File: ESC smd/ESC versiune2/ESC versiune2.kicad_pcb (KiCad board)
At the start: 2 copper layers, 115.8 x 79.8 mm, 96 parts, among them J1 Conn_01x03, J2 Conn_01x03, J3 Conn_01x03, J4 Conn_01x03, J5 Conn_01x02, J6 Conn_01x03, J7 Conn_01x02, Q3 IRLB8721PBF, Q4 IRLB8721PBF, Q5 IRLB8721PBF, Q6 IRLB8721PBF, Q7 IRLB8721PBF, Q8 IRLB8721PBF, U1 L7805, U2 ACS711xLCTR-12AB, U3 LP2950-3.3_TO92, U4 IR2101, U5 IR2101, U6 IR2101, U7 LM393, U8 LM393

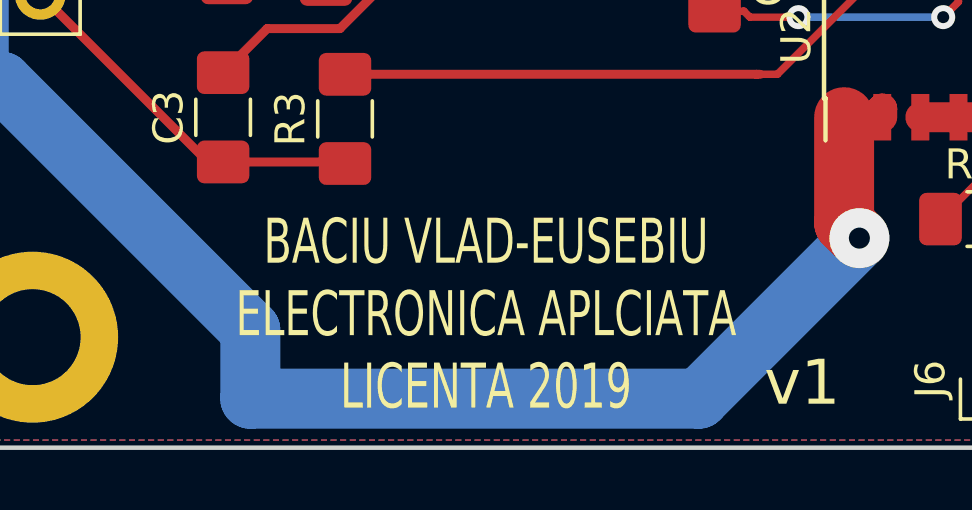
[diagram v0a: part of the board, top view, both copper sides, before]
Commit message: SMD version
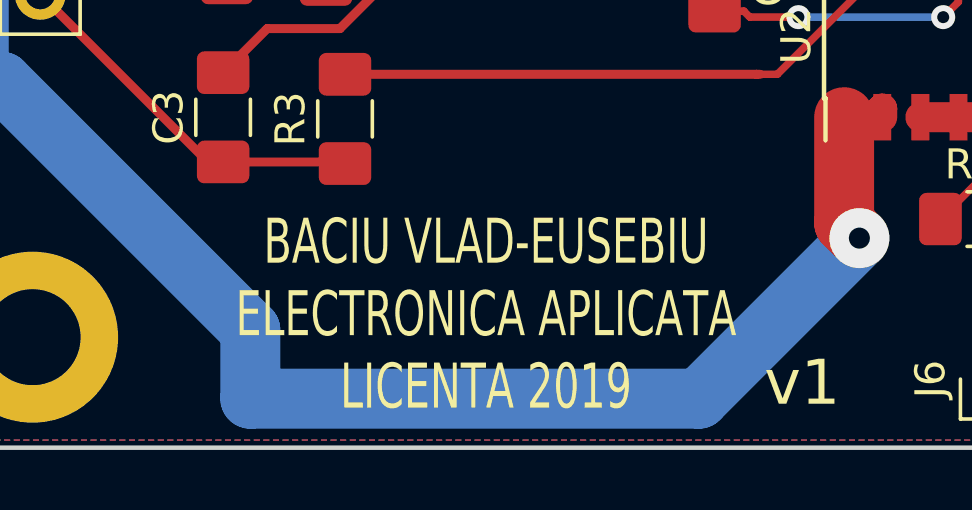
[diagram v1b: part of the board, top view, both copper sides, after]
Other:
- board text added: "BACIU VLAD-EUSEBIU ELECTRONICA APLICATA LICENTA 2019"
- board text removed: "BACIU VLAD-EUSEBIU ELECTRONICA APLCIATA LICENTA 2019"
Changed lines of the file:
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@@
     (effects (font (size 1.5 1) (thickness 0.25)))
   )
-  (gr_text "BACIU VLAD-EUSEBIU\nELECTRONICA APLCIATA\nLICENTA 2019" (at 75.819 126.873) (layer F.SilkS)
+  (gr_text "BACIU VLAD-EUSEBIU\nELECTRONICA APLICATA\nLICENTA 2019" (at 75.819 126.873) (layer F.SilkS)
     (effects (font (size 1.5 1) (thickness 0.25)))
   )
